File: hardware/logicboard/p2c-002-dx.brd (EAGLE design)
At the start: 91 x 55 mm, 50 parts, among them IC1 74LS07N, K1 G5V1, T1 2SC1815

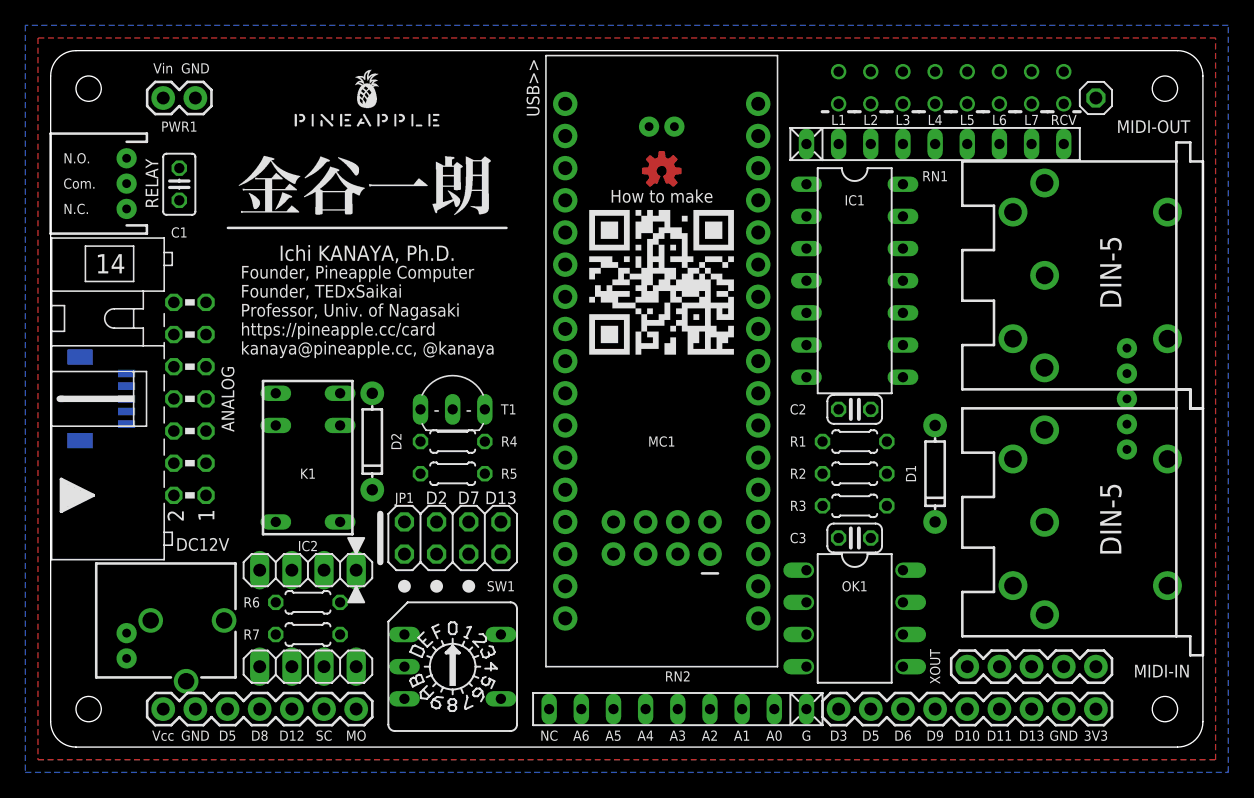
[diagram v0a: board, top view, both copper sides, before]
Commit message: Removed unnecessary parts from DX board.
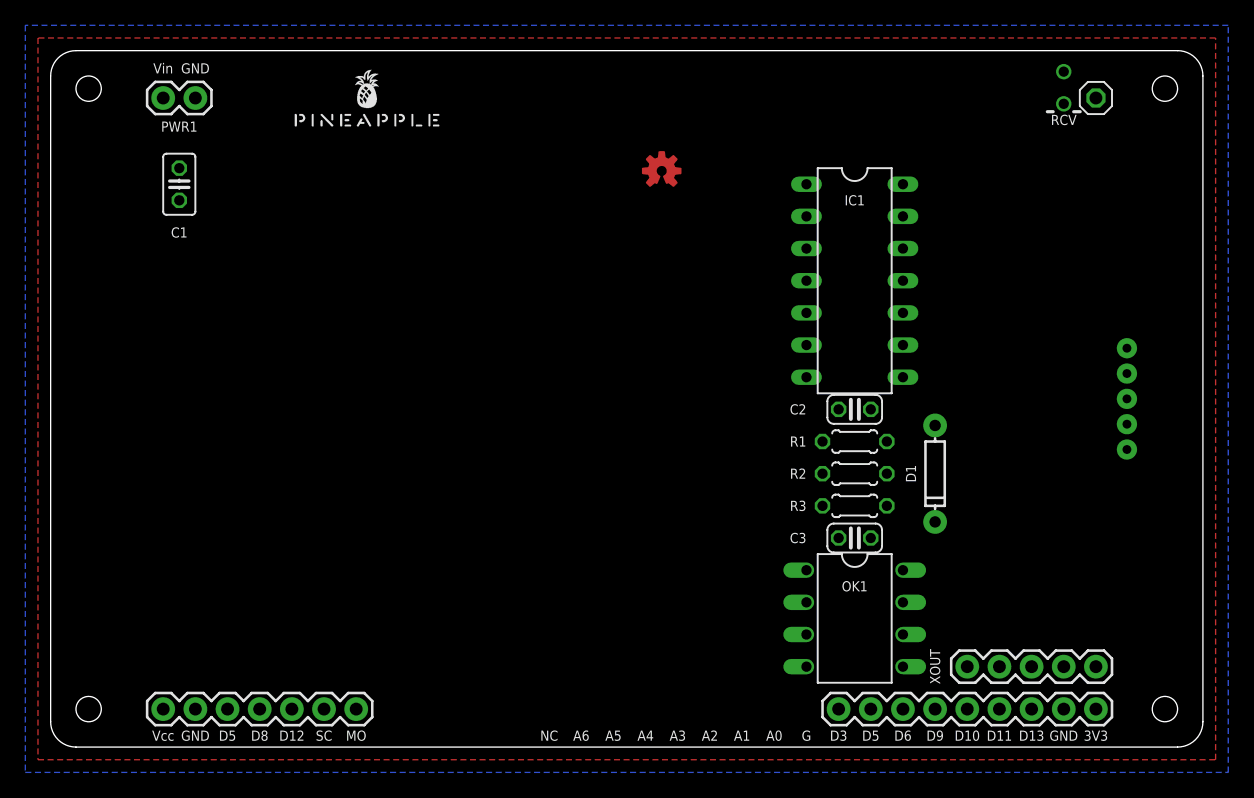
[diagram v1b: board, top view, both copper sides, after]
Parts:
- removed A, B: (no value), pinhead:1X04
- removed ANALOG: (no value), con-ml:ML14L
- removed D2: (no value), SparkFun-DiscreteSemi:DIODE-1N4148
- removed DC12V: POWER_JACKPTH_BREAD, SparkFun-Connectors:POWER_JACK_PTH_BREAD
- removed GND: (no value), SparkFun-Connectors:2X4
- removed I2C: (no value), SparkFun-Connectors:1X05_1MM_RA
- removed JP1: (no value), pinhead:2X04
- removed K1: G5V1, relay:G5V1
- removed L1, L2, L3, L4, L5, L6, L7: (no value), SparkFun-LED:LED_3MM-NS
- removed MIDI-IN, MIDI-OUT: DIN5, SparkFun-Connectors:DIN5-RA-PTH
- removed PWR2, RST: (no value), SparkFun-Connectors:JST-2-PTH
- removed R4, R5: 10k, resistor:0204/5
- removed R6, R7: 6.8k, resistor:0204/5
- removed RELAY: (no value), SparkFun-Connectors:JST-3-PTH
- removed RN1: 330, resistor-net:RN-9
- removed RN2: 10k, resistor-net:RN-9
- removed SW1: (no value), switch-dil:A1353HEX
- removed T1: 2SC1815, transistor:TO92-ECB
- removed U$2: ARDUINOMICRO, adafruit:ARDUINOMICRO
- removed U$3: KANAYA768_SILK, pineapple:KANAYA768_SILK
- removed U$4: CARDQRCODE450_SILK, pineapple:CARDQRCODE450_SILK
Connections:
- removed net ANLG_0: ANALOG.2, RN2.2, U$2.P$31
- removed net ANLG_1: ANALOG.4, RN2.3, U$2.P$30
- removed net ANLG_2: ANALOG.6, RN2.4, U$2.P$29
- removed net ANLG_3: ANALOG.8, RN2.5, U$2.P$28
- removed net ANLG_4: ANALOG.10, RN2.6, U$2.P$27
- removed net ANLG_5: ANALOG.12, RN2.7, U$2.P$26
- removed net ANLG_6: ANALOG.14, RN2.8, U$2.P$9
- removed net I2CENABLE: B.1, JP1.2
- removed net LED1K: L1.K, RN1.2
- removed net LED2K: L2.K, RN1.3
- removed net LED3K: L3.K, RN1.4
- removed net LED4K: L4.K, RN1.5
- removed net LED5K: L5.K, RN1.6
- removed net LED6K: L6.K, RN1.7
- removed net LED7K: L7.K, RN1.8
- removed net RELAYCOM: K1.5, K1.6, RELAY.2
- removed net RELAYDRIVE: R4.2, R5.1, T1.B
- removed net RELAYNC: K1.1, RELAY.3
- removed net RELAYNO: K1.10, RELAY.1
- removed net RELAYTR: D2.A, K1.9, T1.C
- removed net RLYDRV: JP1.7, R5.2
- removed net RST: RST.1, U$2.P$22
- removed net SCL: B.3, I2C.3
- removed net SDA: B.2, I2C.4
- removed net SW0: JP1.3, SW1.1
- removed net SW1: JP1.5, SW1.2
- removed net SW_0: A.2, JP1.4, R7.1, U$2.P$11
- removed net SW_1: I2C.2, JP1.6, U$2.P$6
- net GND: no longer A.4, DC12V.GND, DC12V.GNDBREAK, GND.1, GND.2, GND.3, GND.4, GND.5, GND.6, GND.7, GND.8, I2C.5, JP1.1, MIDI-OUT.2, PWR2.2, R4.1, RN1.1, RN2.1, RST.2, SW1.C, T1.E, U$2.P$12, U$2.P$21
- net MIDIIN: no longer U$2.P$14
- net MIDIIN+: no longer MIDI-IN.4
- net MIDIIN-: no longer MIDI-IN.5
- net MIDIOUT: no longer U$2.P$15
- net MIDIOUT+: no longer MIDI-OUT.4
- net MIDIOUT-: no longer MIDI-OUT.5
- net MOSI: no longer U$2.P$17
- net N$1: no longer RN1.9
- net PWM_0: no longer A.3, L1.A, R6.1, U$2.P$10
- net PWM_1: no longer L2.A, U$2.P$8
- net PWM_2: no longer L3.A, U$2.P$7
- net PWM_3: no longer L4.A, U$2.P$4
- net PWM_4: no longer L5.A, U$2.P$3
- net PWM_5: no longer L6.A, U$2.P$2
- net PWM_6: no longer JP1.8, L7.A, U$2.P$34
- net SCLK: no longer U$2.P$18
- net SW_2: no longer SW1.4, U$2.P$5
- net SW_3: no longer SW1.8, U$2.P$1
- net VCC: no longer A.1, ANALOG.1, ANALOG.11, ANALOG.13, ANALOG.3, ANALOG.5, ANALOG.7, ANALOG.9, D2.C, K1.2, R6.2, R7.2, U$2.P$23
- net VDD: no longer B.4, I2C.1, U$2.P$33
- net VIN: no longer DC12V.PWR, PWR2.1, U$2.P$20
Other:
- board text removed: "Com."
- board text removed: "D2"
- board text removed: "D7"
- board text removed: "Founder, Pineapple Computer Founder, TEDxSaikai Professor, Univ. of Nagasaki https://pineapple.cc/card kanaya@pineapple.cc, @kanaya"
- board text removed: "How to make"
- board text removed: "IC2"
- board text removed: "Ichi KANAYA, Ph.D."
- board text removed: "MC1"
- board text removed: "MC1: Arduino Micro 5V SW1: Comp. HEX Con 5V: Pin 2p Con Analog: ML 14p Con DC: DC Jack Con Digital: Pin 9p Con GND: Pin 2x4p Con Lightdrive: Pin 7p Con I2C: SH 5p Con MIDI: DIN 5p/PH 5p Con Relay: PH 3p Con RST: PH 2p Con XOUT: Pin 5p Pogo: Pin 1p"
- board text removed: "N.C."
- board text removed: "N.O."
- board text removed: "Pineapple IIc 1.2.0"
- board text removed: "R1-3: 220 R4-5: 10k R6-7: 6.8k RN1: 330 RN2: 10k C1: 0.1u C2-3: 0.01u K1: G5V-1 D1-2: 1N4148 LED1-8: If20m T1: 2SC1815 OK1: TLP552 IC1: 74LS07 IC2: PCA9517ADP"
- board text removed: "USB>>"

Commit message: Fixed QR code.
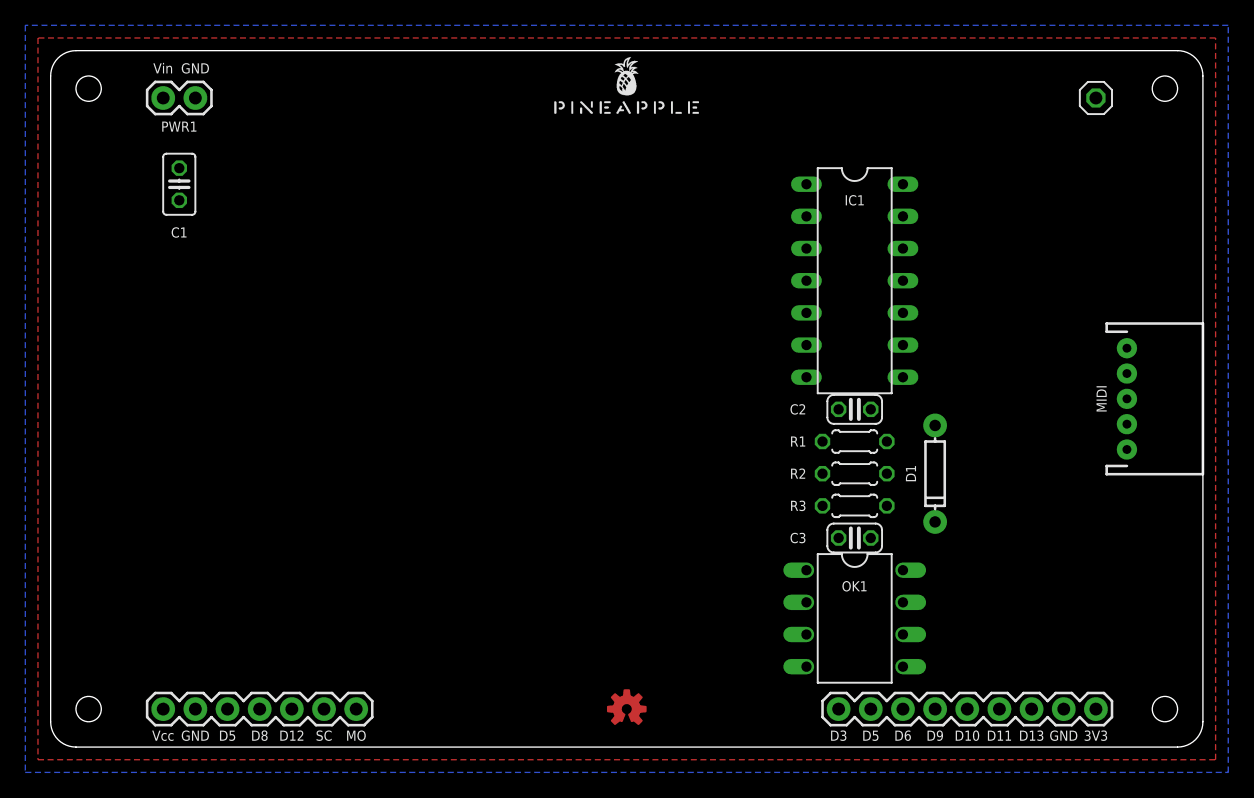
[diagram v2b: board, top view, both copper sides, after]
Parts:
- removed RCV: (no value), SparkFun-LED:LED_3MM-NS
- removed XOUT: (no value), SparkFun-Connectors:1X05
- moved LOGO1 42.6 mm to (45.5, 3.00)
- moved U$1 20.5 mm to (45.5, 50.0)
- flipped MIDI to the top, turned to 270 degrees
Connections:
- removed net MIDIIN: OK1.6, RCV.A
- removed net MIDIOUT: IC1.1, IC1.11, IC1.13, IC1.3, IC1.5, IC1.9
- removed net MOSI: LIGHTDRIVE.7
- removed net PWM_0: DIGITAL.9
- removed net PWM_1: DIGITAL.8, LIGHTDRIVE.3
- removed net PWM_2: DIGITAL.7
- removed net PWM_3: DIGITAL.6
- removed net PWM_4: DIGITAL.5
- removed net PWM_5: DIGITAL.4
- removed net PWM_6: DIGITAL.3
- removed net SCLK: LIGHTDRIVE.6
- removed net SW_2: LIGHTDRIVE.4
- removed net SW_3: LIGHTDRIVE.5
- removed net VDD: DIGITAL.1
- removed net VIN: PWR1.1
- removed net X1: IC1.4, XOUT.1
- removed net X2: IC1.6, XOUT.2
- removed net X3: IC1.8, XOUT.3
- removed net X4: IC1.10, XOUT.4
- removed net X5: IC1.12, XOUT.5
- net GND: now also IC1.11, IC1.13, IC1.3, IC1.5, IC1.9; no longer DIGITAL.2, LIGHTDRIVE.2, MIDI.2, PWR1.2
- net MIDIIN+: no longer MIDI.4
- net MIDIIN-: no longer MIDI.5
- net MIDIOUT+: no longer MIDI.1
- net MIDIOUT-: no longer MIDI.3
- net N$1: now also IC1.1; no longer RCV.K
- net VCC: no longer LIGHTDRIVE.1
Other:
- board text removed: "3"
- board text removed: "4"
- board text removed: "5"
- board text removed: "A0"
- board text removed: "A1"
- board text removed: "A2"
- board text removed: "A3"
- board text removed: "A4"
- board text removed: "A5"
- board text removed: "A6"
- board text removed: "ANALOG"
- board text removed: "G"
- board text removed: "IN"
- board text removed: "NC"
- board text removed: "OUT"
